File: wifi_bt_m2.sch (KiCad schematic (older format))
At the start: 24 parts, among them J1502 M.2_Key_E, Q1501 FDV301N, Q1502 FDV301N, SW1501 WWAN_HKS, U1502 74AUP2G00, U1504 NTB0104GU12, U1702 NTB0104GU12

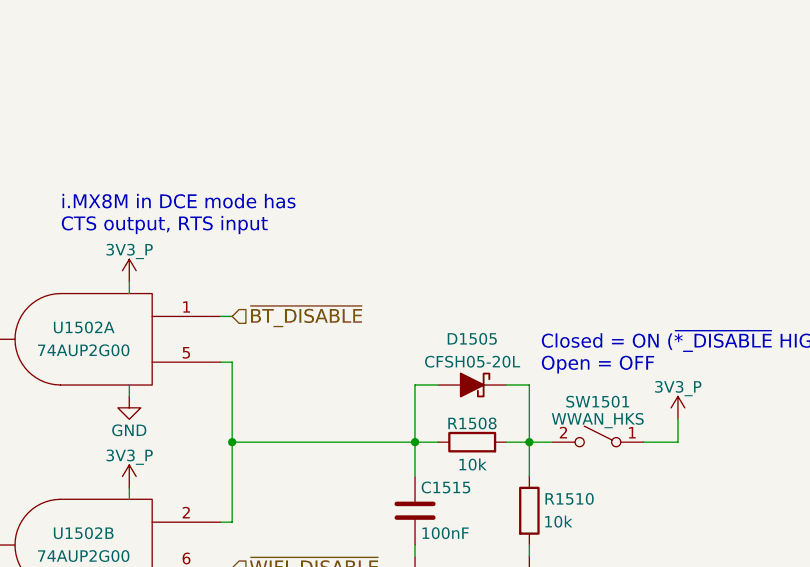
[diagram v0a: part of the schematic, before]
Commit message: Add HDMI schematic and connector footprint (using SMD type D/micro-HDMI receptacle)
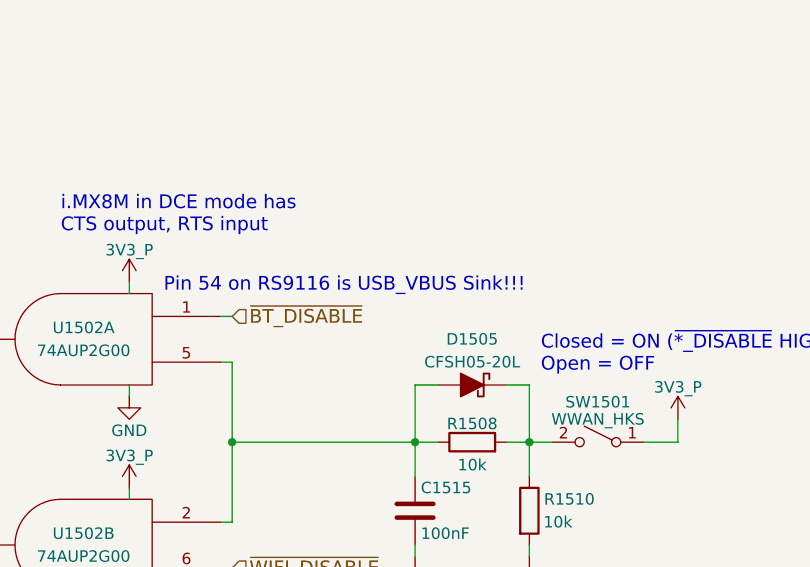
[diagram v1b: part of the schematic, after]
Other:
- note added: "Pin 54 on RS9116 is USB_VBUS Sink!!!"
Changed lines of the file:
@@
 $Descr A4 11693 8268
 encoding utf-8
-Sheet 17 17
+Sheet 17 18
 Title "WLAN+BT M.2"
 Date "2018-05-02"
@@
 	5350 1500 5250 1500
 $Comp
-L GND #PWR0279
+L GND #PWR0282
 U 1 1 5B01D9F9
 P 5300 5050
-F 0 "#PWR0279" H 5300 4800 50  0001 C CNN
+F 0 "#PWR0282" H 5300 4800 50  0001 C CNN
 F 1 "GND" H 5300 4900 50  0000 C CNN
 F 2 "" H 5300 5050 50  0001 C CNN
@@
 Connection ~ 5300 5000
 $Comp
-L GND #PWR0280
+L GND #PWR0283
 U 1 1 5B01E5BE
 P 5900 5050
-F 0 "#PWR0280" H 5900 4800 50  0001 C CNN
+F 0 "#PWR0283" H 5900 4800 50  0001 C CNN
 F 1 "GND" H 5900 4900 50  0000 C CNN
 F 2 "" H 5900 5050 50  0001 C CNN
@@
 	5900 2150 5900 5050
 $Comp
-L 3V3_P #PWR0281
+L 3V3_P #PWR0284
 U 1 1 5B01E6B8
 P 5950 1300
-F 0 "#PWR0281" H 5950 1150 50  0001 C CNN
+F 0 "#PWR0284" H 5950 1150 50  0001 C CNN
 F 1 "3V3_P" H 5950 1440 50  0000 C CNN
 F 2 "" H 5950 1300 50  0001 C CNN
@@
 $EndComp
 $Comp
-L 3V3_P #PWR0282
+L 3V3_P #PWR0285
 U 1 1 5B0C3C8A
 P 10150 3900
-F 0 "#PWR0282" H 10150 3750 50  0001 C CNN
+F 0 "#PWR0285" H 10150 3750 50  0001 C CNN
 F 1 "3V3_P" H 10150 4040 50  0000 C CNN
 F 2 "" H 10150 3900 50  0001 C CNN
@@
 NoConn ~ 6500 3750
 $Comp
-L 3V3_P #PWR0283
+L 3V3_P #PWR0286
 U 1 1 5B0D90EE
 P 7750 3300
-F 0 "#PWR0283" H 7750 3150 50  0001 C CNN
+F 0 "#PWR0286" H 7750 3150 50  0001 C CNN
 F 1 "3V3_P" H 7750 3440 50  0000 C CNN
 F 2 "" H 7750 3300 50  0001 C CNN
@@
 	7750 3300 7750 3350
 $Comp
-L GND #PWR0284
+L GND #PWR0287
 U 1 1 5B0D91C5
 P 7750 4700
-F 0 "#PWR0284" H 7750 4450 50  0001 C CNN
+F 0 "#PWR0287" H 7750 4450 50  0001 C CNN
 F 1 "GND" H 7750 4550 50  0000 C CNN
 F 2 "" H 7750 4700 50  0001 C CNN
@@
 Connection ~ 4550 2400
 $Comp
-L 1V8_P #PWR0285
+L 1V8_P #PWR0288
 U 1 1 5AEFAF82
 P 4550 2000
-F 0 "#PWR0285" H 4550 1850 50  0001 C CNN
+F 0 "#PWR0288" H 4550 1850 50  0001 C CNN
 F 1 "1V8_P" H 4550 2140 50  0000 C CNN
 F 2 "" H 4550 2000 50  0001 C CNN
@@
 $EndComp
 $Comp
-L 1V8_P #PWR0286
+L 1V8_P #PWR0289
 U 1 1 5AEB9155
 P 7000 5050
-F 0 "#PWR0286" H 7000 4900 50  0001 C CNN
+F 0 "#PWR0289" H 7000 4900 50  0001 C CNN
 F 1 "1V8_P" H 7000 5190 50  0000 C CNN
 F 2 "" H 7000 5050 50  0001 C CNN
@@
 TODO!!!\nverify if translators\nwith PWR_EN is needed!
 $Comp
-L 3V3_P #PWR0287
+L 3V3_P #PWR0290
 U 1 1 5AF2CD0D
 P 7750 4200
-F 0 "#PWR0287" H 7750 4050 50  0001 C CNN
+F 0 "#PWR0290" H 7750 4050 50  0001 C CNN
 F 1 "3V3_P" H 7750 4340 50  0000 C CNN
 F 2 "" H 7750 4200 50  0001 C CNN
@@
 	7750 4200 7750 4250
 $Comp
-L GND #PWR0288
+L GND #PWR0291
 U 1 1 5AF2CDB4
 P 7750 3800
-F 0 "#PWR0288" H 7750 3550 50  0001 C CNN
+F 0 "#PWR0291" H 7750 3550 50  0001 C CNN
 F 1 "GND" H 7750 3650 50  0000 C CNN
 F 2 "" H 7750 3800 50  0001 C CNN
@@
 $EndComp
 $Comp
-L GND #PWR0289
+L GND #PWR0292
 U 1 1 5AF3C984
 P 9000 4500
-F 0 "#PWR0289" H 9000 4250 50  0001 C CNN
+F 0 "#PWR0292" H 9000 4250 50  0001 C CNN
 F 1 "GND" H 9000 4350 50  0000 C CNN
 F 2 "" H 9000 4500 50  0001 C CNN
@@
 $EndComp
 $Comp
-L GND #PWR0290
+L GND #PWR0293
 U 1 1 5AF3C98A
 P 9500 4500
-F 0 "#PWR0290" H 9500 4250 50  0001 C CNN
+F 0 "#PWR0293" H 9500 4250 50  0001 C CNN
 F 1 "GND" H 9500 4350 50  0000 C CNN
 F 2 "" H 9500 4500 50  0001 C CNN
@@
 $EndComp
 $Comp
-L 1V8_P #PWR0291
+L 1V8_P #PWR0294
 U 1 1 5AEBC081
 P 9400 5050
-F 0 "#PWR0291" H 9400 4900 50  0001 C CNN
+F 0 "#PWR0294" H 9400 4900 50  0001 C CNN
 F 1 "1V8_P" H 9400 5190 50  0000 C CNN
 F 2 "" H 9400 5050 50  0001 C CNN
@@
 $EndComp
 $Comp
-L GND #PWR0292
+L GND #PWR0295
 U 1 1 5B2489BD
 P 6350 6200
-F 0 "#PWR0292" H 6350 5950 50  0001 C CNN
+F 0 "#PWR0295" H 6350 5950 50  0001 C CNN
 F 1 "GND" H 6350 6050 50  0000 C CNN
 F 2 "" H 6350 6200 50  0001 C CNN
@@
 $EndComp
 $Comp
-L GND #PWR0293
+L GND #PWR0296
 U 1 1 5B2489DB
 P 4600 6200
-F 0 "#PWR0293" H 4600 5950 50  0001 C CNN
+F 0 "#PWR0296" H 4600 5950 50  0001 C CNN
 F 1 "GND" H 4600 6050 50  0000 C CNN
 F 2 "" H 4600 6200 50  0001 C CNN
@@
 	4450 5750 5300 5750
 $Comp
-L GND #PWR0294
+L GND #PWR0297
 U 1 1 5B2489F2
 P 5400 7550
-F 0 "#PWR0294" H 5400 7300 50  0001 C CNN
+F 0 "#PWR0297" H 5400 7300 50  0001 C CNN
 F 1 "GND" H 5400 7400 50  0000 C CNN
 F 2 "" H 5400 7550 50  0001 C CNN
@@
 BCLK
 $Comp
-L 3V3_P #PWR0295
+L 3V3_P #PWR0298
 U 1 1 5B248A11
 P 6200 5700
-F 0 "#PWR0295" H 6200 5550 50  0001 C CNN
+F 0 "#PWR0298" H 6200 5550 50  0001 C CNN
 F 1 "3V3_P" H 6200 5840 50  0000 C CNN
 F 2 "" H 6200 5700 50  0001 C CNN
@@
 $EndComp
 $Comp
-L 1V8_P #PWR0296
+L 1V8_P #PWR0299
 U 1 1 5B248A1D
 P 4950 5700
-F 0 "#PWR0296" H 4950 5550 50  0001 C CNN
+F 0 "#PWR0299" H 4950 5550 50  0001 C CNN
 F 1 "1V8_P" H 4950 5840 50  0000 C CNN
 F 2 "" H 4950 5700 50  0001 C CNN
@@
 $EndComp
 $Comp
-L GND #PWR0297
+L GND #PWR0300
 U 1 1 5B337EDE
 P 3200 6200
-F 0 "#PWR0297" H 3200 5950 50  0001 C CNN
+F 0 "#PWR0300" H 3200 5950 50  0001 C CNN
 F 1 "GND" H 3200 6050 50  0000 C CNN
 F 2 "" H 3200 6200 50  0001 C CNN
@@
 $EndComp
 $Comp
-L GND #PWR0298
+L GND #PWR0301
 U 1 1 5B337EFC
 P 1450 6200
-F 0 "#PWR0298" H 1450 5950 50  0001 C CNN
+F 0 "#PWR0301" H 1450 5950 50  0001 C CNN
 F 1 "GND" H 1450 6050 50  0000 C CNN
 F 2 "" H 1450 6200 50  0001 C CNN
@@
 	1300 5750 2150 5750
 $Comp
-L GND #PWR0299
+L GND #PWR0302
 U 1 1 5B337F13
 P 2250 7550
-F 0 "#PWR0299" H 2250 7300 50  0001 C CNN
+F 0 "#PWR0302" H 2250 7300 50  0001 C CNN
 F 1 "GND" H 2250 7400 50  0000 C CNN
 F 2 "" H 2250 7550 50  0001 C CNN
@@
 	2650 7100 2700 7100
 $Comp
-L 3V3_P #PWR0300
+L 3V3_P #PWR0303
 U 1 1 5B337F23
 P 3050 5700
-F 0 "#PWR0300" H 3050 5550 50  0001 C CNN
+F 0 "#PWR0303" H 3050 5550 50  0001 C CNN
 F 1 "3V3_P" H 3050 5840 50  0000 C CNN
 F 2 "" H 3050 5700 50  0001 C CNN
@@
 $EndComp
 $Comp
-L 1V8_P #PWR0301
+L 1V8_P #PWR0304
 U 1 1 5B337F29
 P 1800 5700
-F 0 "#PWR0301" H 1800 5550 50  0001 C CNN
+F 0 "#PWR0304" H 1800 5550 50  0001 C CNN
 F 1 "1V8_P" H 1800 5840 50  0000 C CNN
 F 2 "" H 1800 5700 50  0001 C CNN
@@
 Wire Wire Line
 	1800 5700 1800 6300
+Text Notes 7900 3350 0    60   ~ 0
+Pin 54 on RS9116 is USB_VBUS Sink!!!
 $EndSCHEMATC

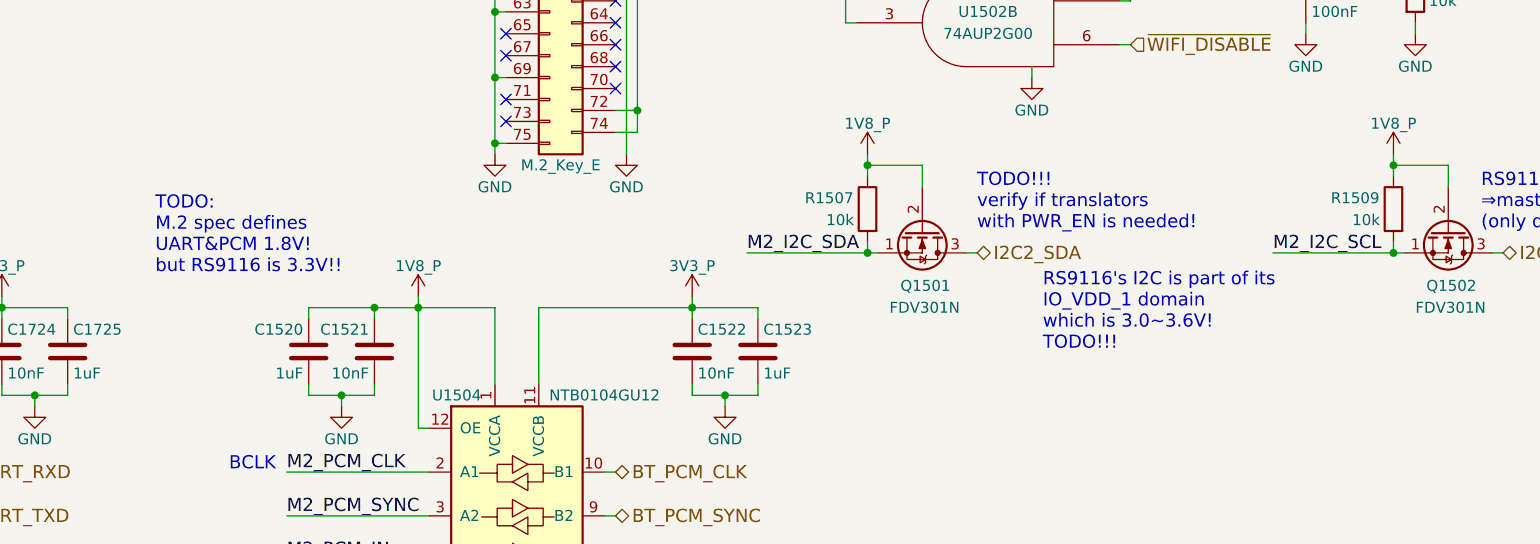
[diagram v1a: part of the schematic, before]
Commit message: Add Proximity+Ambient Light sensor and 9-axis IMU circuits to the "sensors" schematic sheet, include the associated footprints and assign them to the respective symbols
The 9-axis IMU is configured to use I2C(1) rather than SPI. Notes are included regarding the IMU's setup. Descriptions of the IMU state that it is "fully compliant with Android" and therefore drivers must be available.
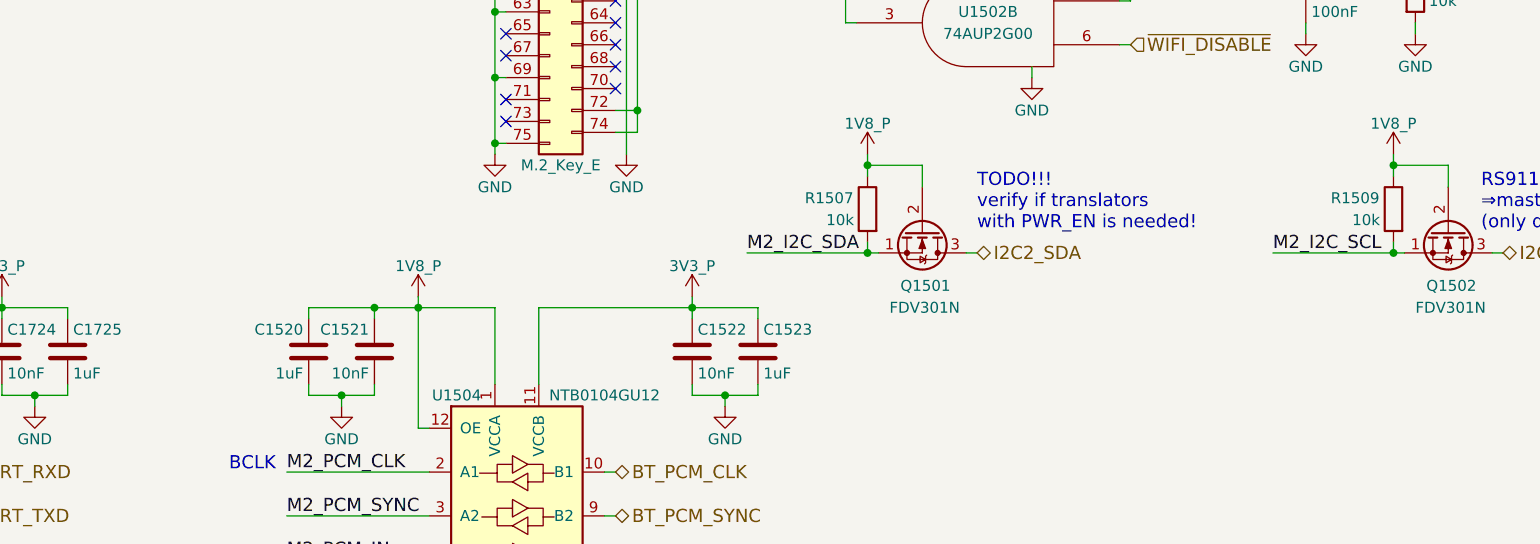
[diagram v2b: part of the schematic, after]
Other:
- note removed: "RS9116's I2C is part of its\nIO_VDD_1 domain\nwhich is 3.0~~3.6V!\nTODO!!!"
- note removed: "TODO:\nM.2 spec defines\nUART&PCM 1.8V!\nbut RS9116 is 3.3V!!"
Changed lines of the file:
@@
 $Descr A4 11693 8268
 encoding utf-8
-Sheet 17 18
+Sheet 17 19
 Title "WLAN+BT M.2"
 Date "2018-05-02"
@@
 Text Notes 9800 5400 0    60   ~ 0
 RS9116 has SCL as output\n⇒master?\n(only device on I2C2 bus)
-Text Notes 7800 5950 0    60   ~ 0
-RS9116's I2C is part of its\nIO_VDD_1 domain\nwhich is 3.0~~3.6V!\nTODO!!!
 Text Notes 9550 3700 0    60   ~ 0
 Closed = ON (~*_DISABLE~ HIGH)\nOpen = OFF
@@
 	1    0    0    -1
 $EndComp
-Text Notes 3750 5600 0    60   ~ 0
-TODO:\nM.2 spec defines\nUART&PCM 1.8V!\nbut RS9116 is 3.3V!!
 Text Label 6650 1650 2    60   ~ 0
 M2_PCM_CLK

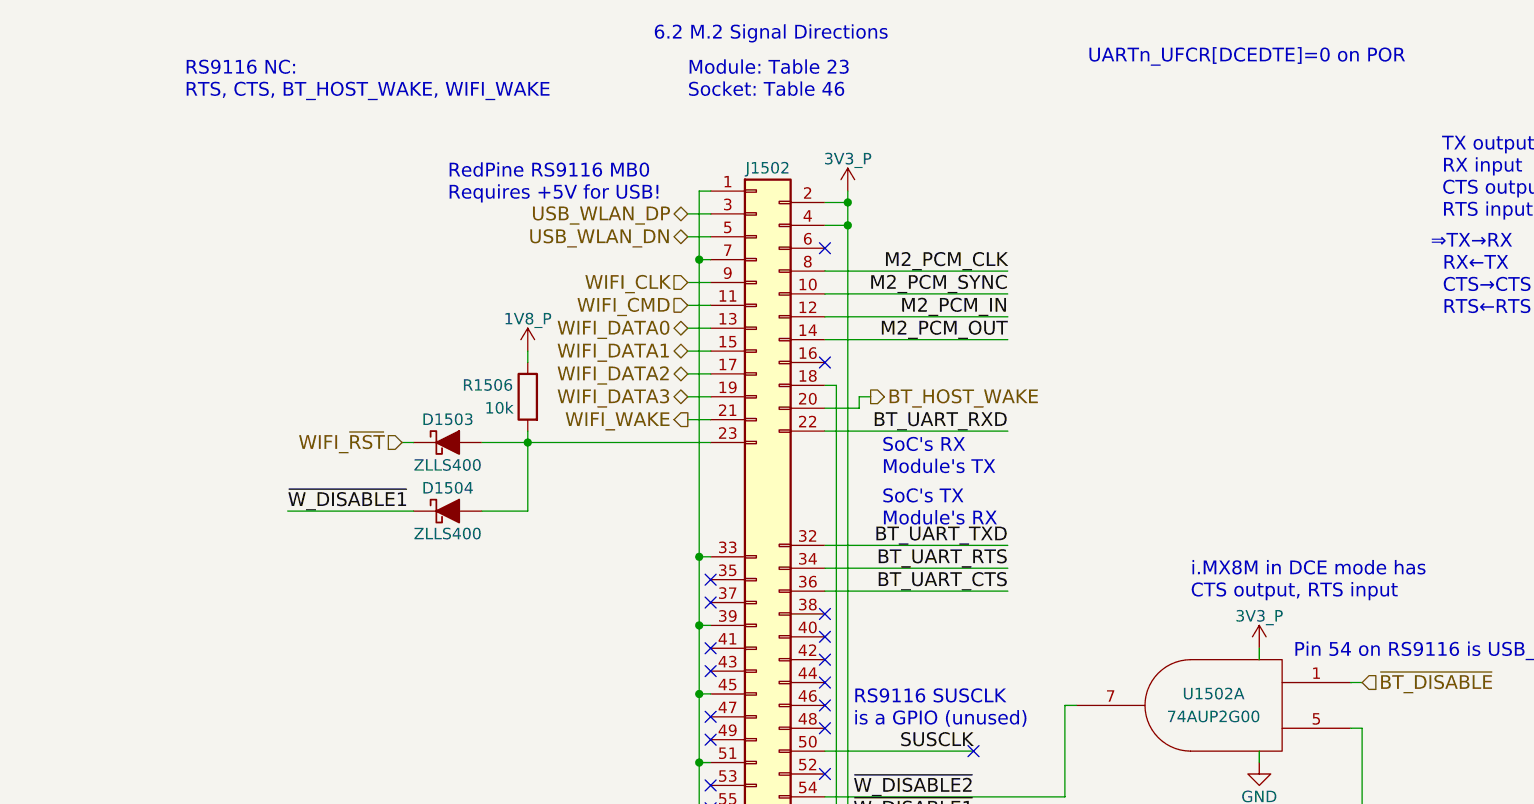
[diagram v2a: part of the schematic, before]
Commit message: Add NOR flash chip schematic, use mini-HDMI (requested) instead of micro and add its corresponding properties and footprint, use 3.5mm CTIA headset jack with through-hole pins rather than an SMD one for extra "mechanical rigidity"
Will likely want to use a USB-C receptacle with through-hole shield pins.
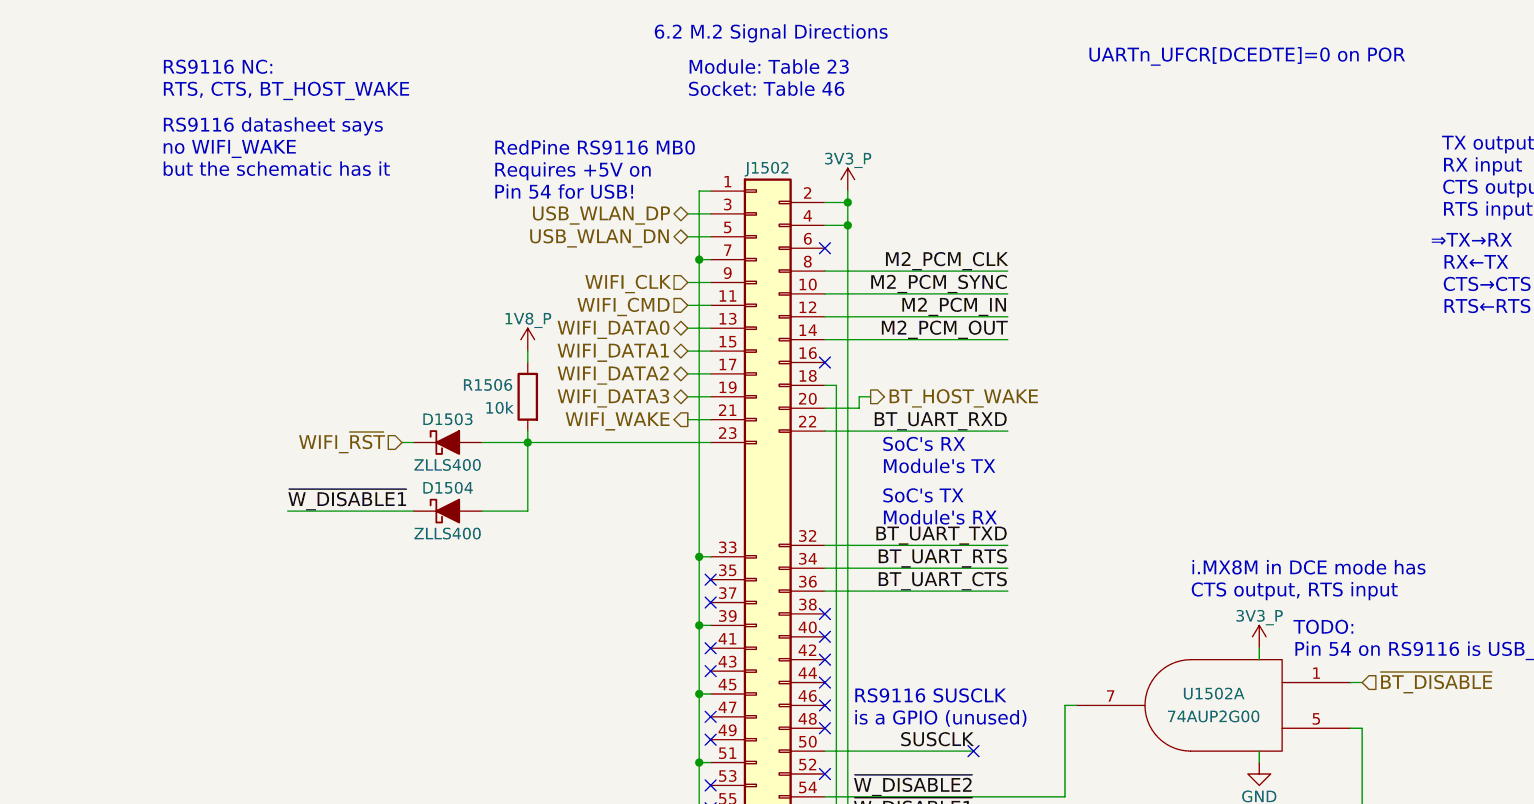
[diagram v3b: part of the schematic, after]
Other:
- note added: "RS9116 NC:\nRTS, CTS, BT_HOST_WAKE"
- note added: "RS9116 datasheet says\nno WIFI_WAKE\nbut the schematic has it"
- note added: "RedPine RS9116 MB0\nRequires +5V on\nPin 54 for USB!"
- note added: "TODO:\nPin 54 on RS9116 is USB_VBUS Sink!!!"
- note removed: "Pin 54 on RS9116 is USB_VBUS Sink!!!"
- note removed: "RS9116 NC:\nRTS, CTS, BT_HOST_WAKE, WIFI_WAKE"
- note removed: "RedPine RS9116 MB0\nRequires +5V for USB!"
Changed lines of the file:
@@
 $Descr A4 11693 8268
 encoding utf-8
-Sheet 17 19
+Sheet 17 20
 Title "WLAN+BT M.2"
-Date "2018-05-02"
+Date "2018-05-14"
 Rev "v0.1.0"
 Comp "Purism SPC"
@@
 Text HLabel 5250 2200 0    60   BiDi ~ 0
 WIFI_DATA3
-Text Notes 4200 1350 0    60   ~ 0
-RedPine RS9116 MB0\nRequires +5V for USB!
-Text Notes 3050 900  0    60   ~ 0
-RS9116 NC:\nRTS, CTS, BT_HOST_WAKE, WIFI_WAKE
+Text Notes 2950 900  0    60   ~ 0
+RS9116 NC:\nRTS, CTS, BT_HOST_WAKE
 Text HLabel 5250 2300 0    60   Output ~ 0
 WIFI_WAKE
@@
 	1800 5700 1800 6300
 Text Notes 7900 3350 0    60   ~ 0
-Pin 54 on RS9116 is USB_VBUS Sink!!!
+TODO:\nPin 54 on RS9116 is USB_VBUS Sink!!!
+Text Notes 4400 1350 0    60   ~ 0
+RedPine RS9116 MB0\nRequires +5V on\nPin 54 for USB!
+Text Notes 2950 1250 0    60   ~ 0
+RS9116 datasheet says\nno WIFI_WAKE\nbut the schematic has it
 $EndSCHEMATC
